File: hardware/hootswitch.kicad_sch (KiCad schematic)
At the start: 60 parts, among them J1 Mini-DIN-4-G, J2 Switch1, J7 Barrel_Jack_MountingPin, J8 POWER, J9 POWSEL, Q1 MMBT3904, Q2 MMBT3904, Q20 MMBT3904, Q3 MMBT3904, Q4 MMBT3904, Q5 MMBT3904, Q6 MMBT3904, Q7 MMBT3904, SW1 Switch1, U1 Pico, U14 LM1117-5.0

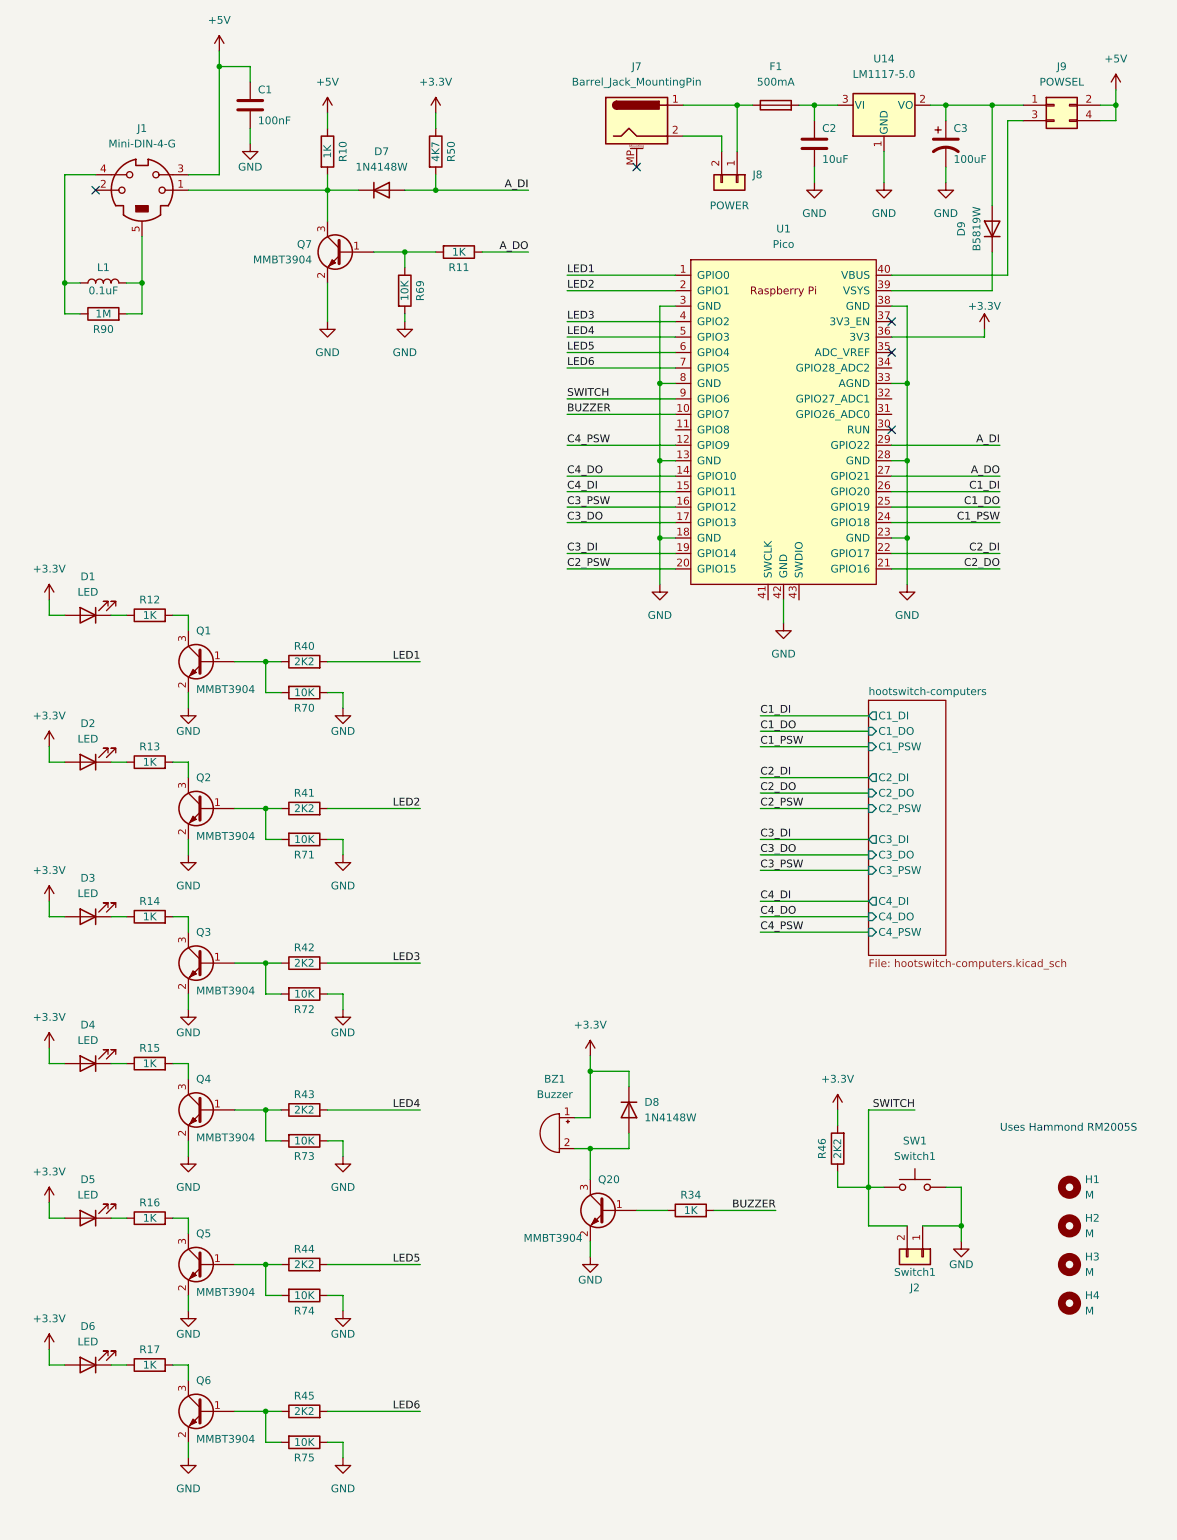
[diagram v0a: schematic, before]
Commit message: Switch to using proper digital isolator for data lines.
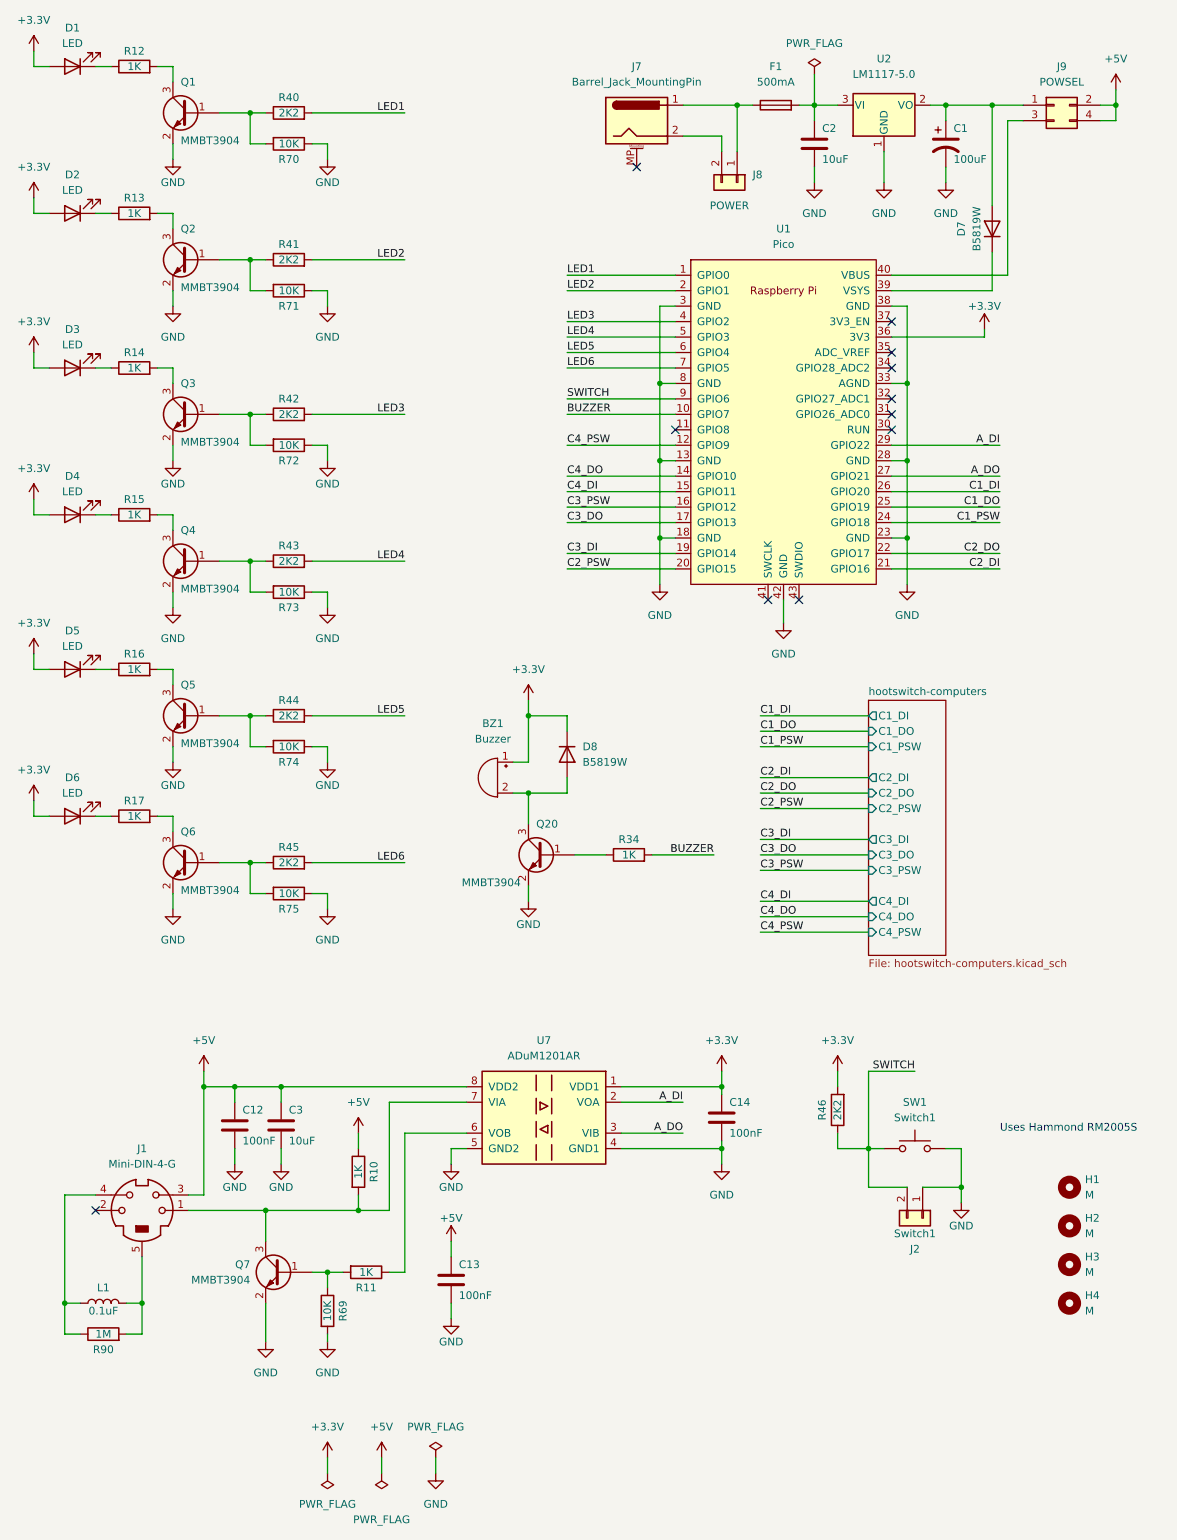
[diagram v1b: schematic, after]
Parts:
- removed D7: 1N4148W, Diode_SMD:D_SOD-123, symbol Diode:1N4148W
- removed R50: 4K7, Resistor_SMD:R_0603_1608Metric, symbol Device:R
- added C13, C14: 100nF, Capacitor_SMD:C_0603_1608Metric, symbol Device:C
- added C3: 10uF, Capacitor_SMD:C_0805_2012Metric, symbol Device:C
- added U7: ADuM1201AR, Package_SO:SOIC-8_3.9x4.9mm_P1.27mm, symbol Isolator:ADuM1201AR
- D8: value 1N4148W -> B5819W
- renumbered C3 to C1, C1 to C12, D9 to D7, U14 to U2
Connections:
- net +3.3V: now also C14.1, U7.1 (VDD1)
- net +5V: now also C13.1, C3.1, U7.8 (VDD2)
- net A_DI: now also U7.2 (VOA)
- net A_DO: now also U7.3 (VIB); no longer R11.1
- net C2_DI: now also U1.21 (GPIO16); no longer U1.22 (GPIO17)
- net C2_DO: now also U1.22 (GPIO17); no longer U1.21 (GPIO16)
- net GND: now also C13.2, C14.2, C3.2, U7.4 (GND1), U7.5 (GND2)
- net at J1.1, Q7.3 (C), R10.2: now also U7.7 (VIA)
- new net: R11.1, U7.6 (VOB)
- no-connect marks 5 -> 11
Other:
- moved on the sheet: BZ1, C12, D1, D2, D3, D4, D5, D6, D8, J1, J2, L1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

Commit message: Refinements for v2024a during BOM creation.
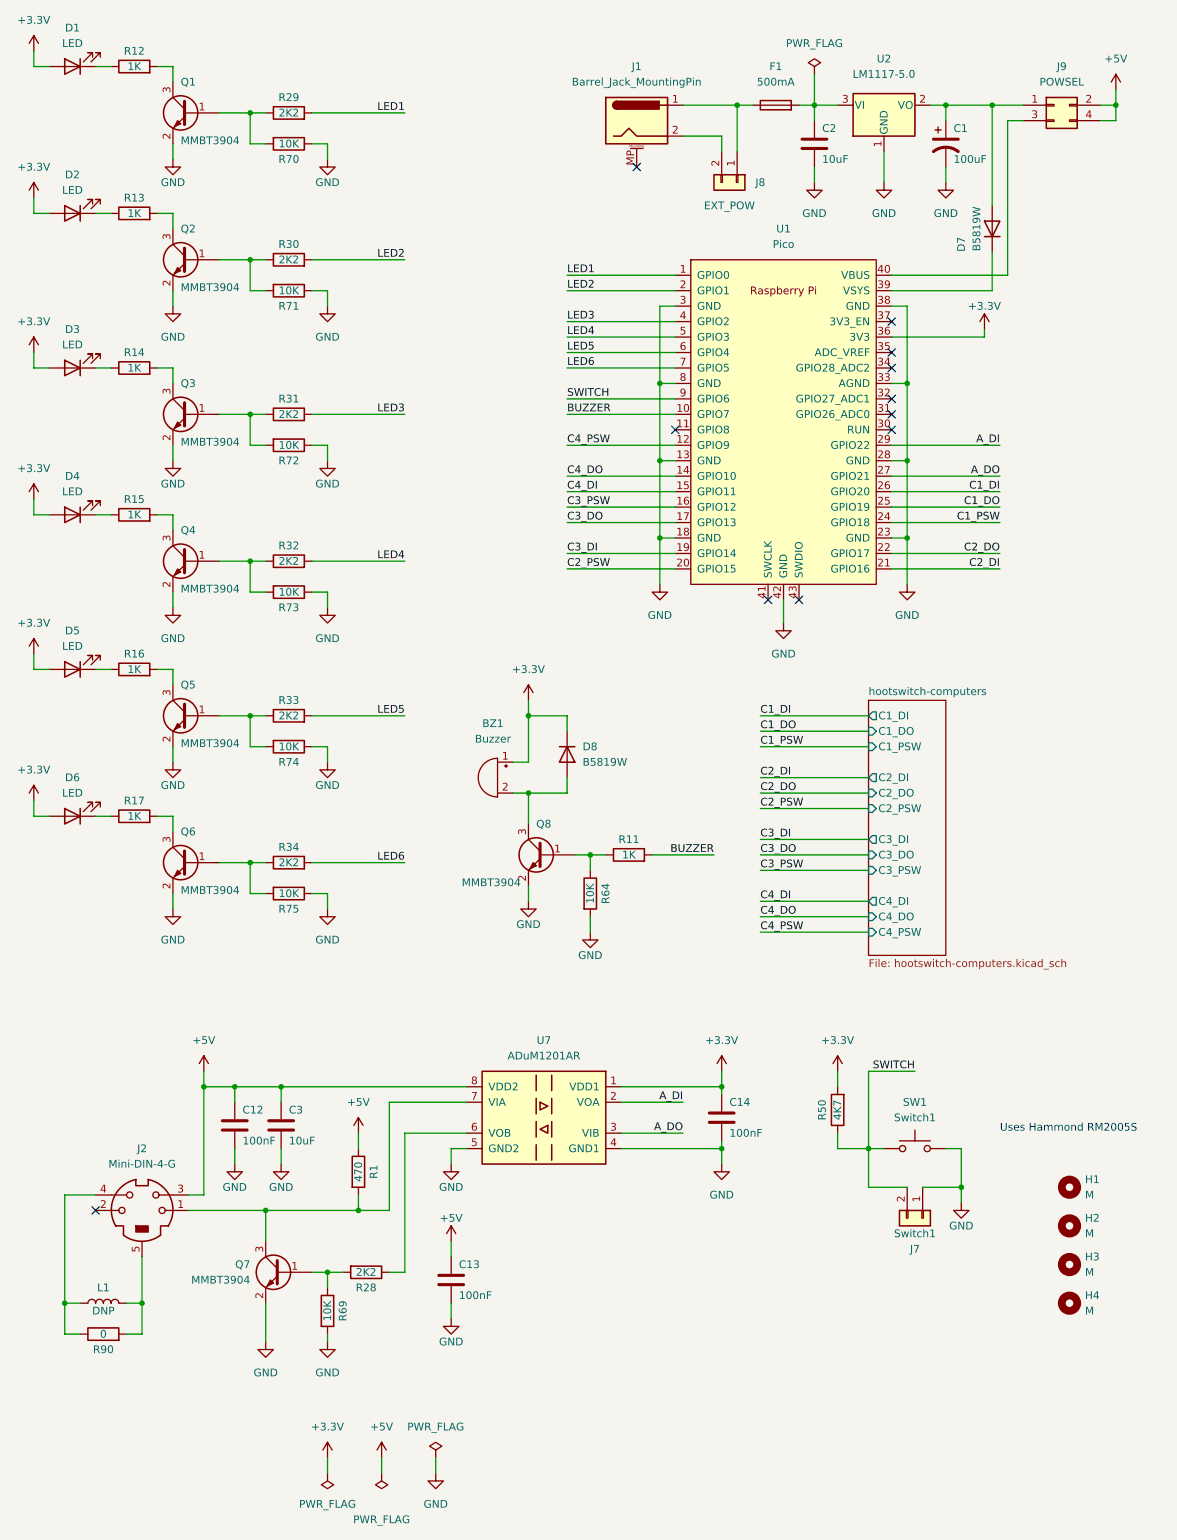
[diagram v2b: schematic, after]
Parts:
- added R64: 10K, Resistor_SMD:R_0603_1608Metric, symbol Device:R
- D7: symbol Simulation_SPICE:DIODE -> Device:D
- D8: symbol Diode:1N4148W -> Device:D
- J8: value POWER -> EXT_POW
- L1: value 0.1uF -> DNP
- R1: renamed from R10; value 1K -> 470
- R28: renamed from R11; value 1K -> 2K2
- R50: renamed from R46; value 2K2 -> 4K7
- R90: value 1M -> 0
- renumbered J7 to J1, J1 to J2, J2 to J7, Q20 to Q8, R34 to R11, R40 to R29, R41 to R30, R42 to R31, R43 to R32, R44 to R33, R45 to R34
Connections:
- net GND: now also R64.2
- net at C1.1, J9.1 (Pin_1), U2.2 (VO): now also D7.2 (A); no longer D7.1 (A)
- net at U1.39 (VSYS): now also D7.1 (K); no longer D7.2 (K)
- net at Q8.1 (B), R11.1: now also R64.1
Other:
- moved on the sheet: D7

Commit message: Add TWI and second DIN connector, update BOM.
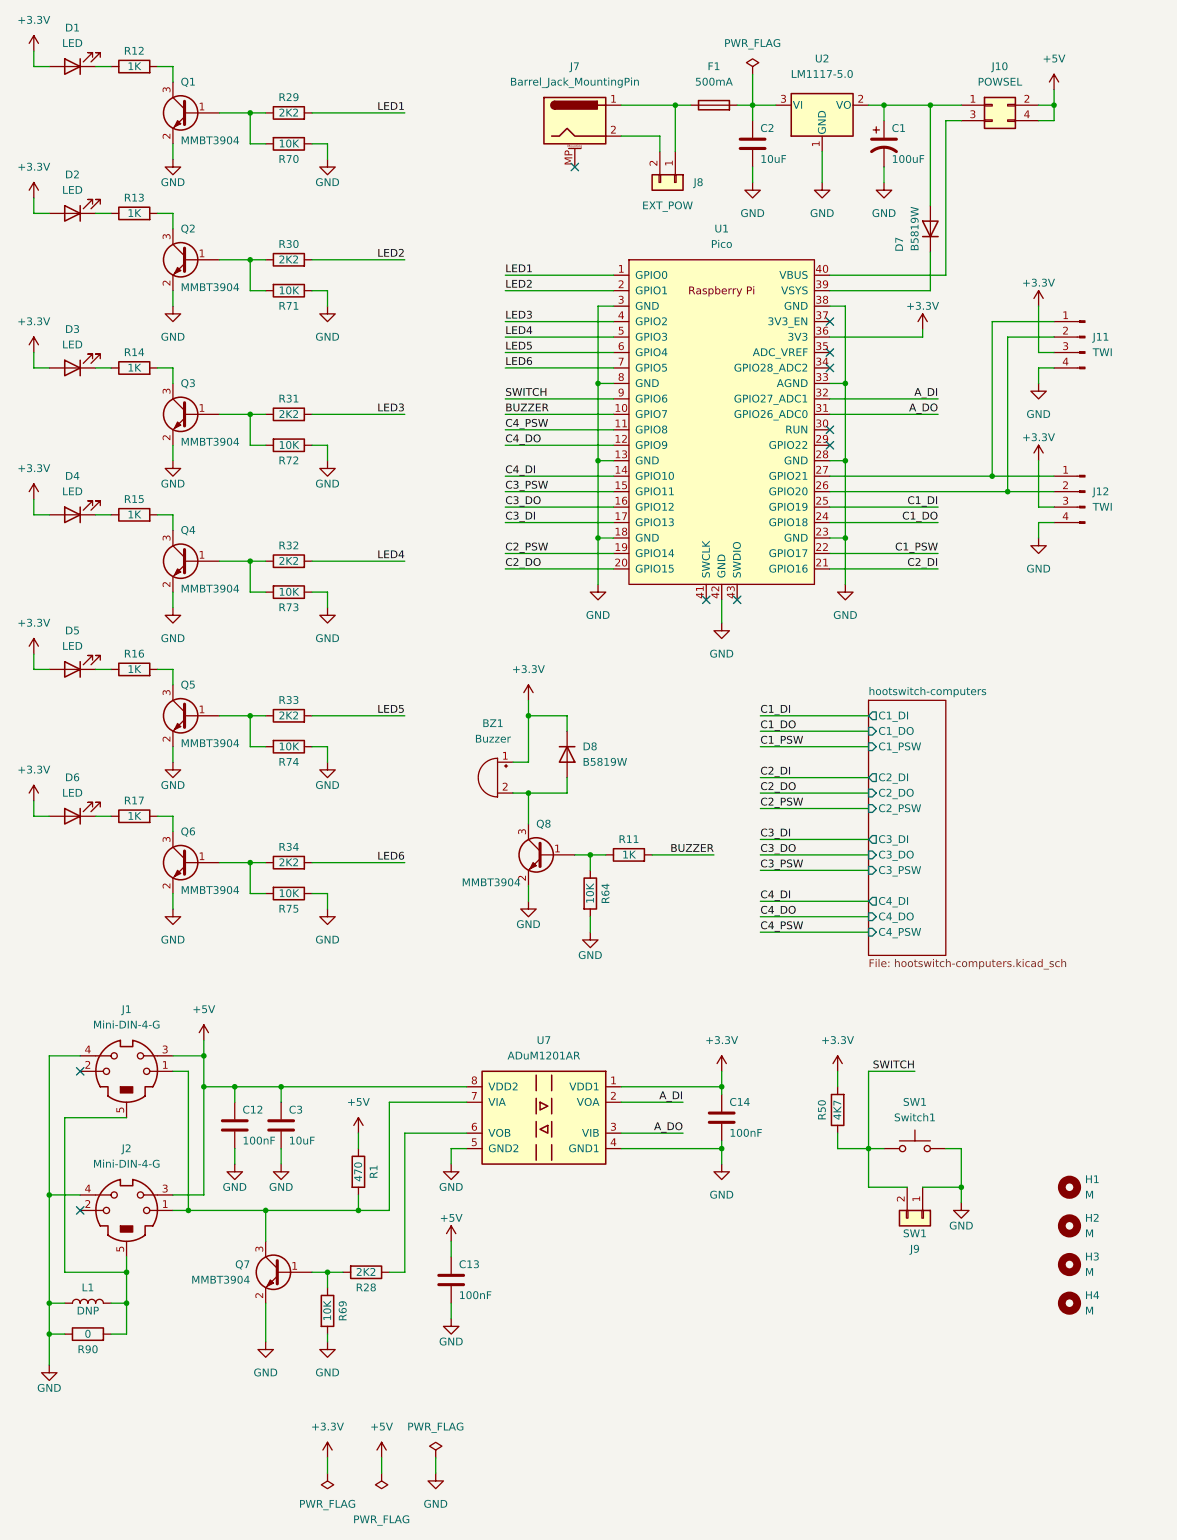
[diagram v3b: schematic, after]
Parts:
- added J1: Mini-DIN-4-G, hootswitch:5749181-1, symbol hootswitch:Mini-DIN-4-G
- added J11: TWI, Connector_JST:JST_SH_BM04B-SRSS-TB_1x04-1MP_P1.00mm_Vertical, symbol Connector:Conn_01x04_Male
- added J12: TWI, Connector_PinHeader_2.54mm:PinHeader_1x04_P2.54mm_Vertical, symbol Connector:Conn_01x04_Male
- J9: renamed from J7; value Switch1 -> SW1
- renumbered J9 to J10, J1 to J7
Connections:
- net +3.3V: now also J11.3 (Pin_3), J12.3 (Pin_3)
- net +5V: now also J1.3
- net A_DI: now also U1.32 (GPIO27_ADC1); no longer U1.29 (GPIO22)
- net A_DO: now also U1.31 (GPIO26_ADC0); no longer U1.27 (GPIO21)
- net C1_DI: now also U1.25 (GPIO19); no longer U1.26 (GPIO20)
- net C1_DO: now also U1.24 (GPIO18); no longer U1.25 (GPIO19)
- net C1_PSW: now also U1.22 (GPIO17); no longer U1.24 (GPIO18)
- net C2_DO: now also U1.20 (GPIO15); no longer U1.22 (GPIO17)
- net C2_PSW: now also U1.19 (GPIO14); no longer U1.20 (GPIO15)
- net C3_DI: now also U1.17 (GPIO13); no longer U1.19 (GPIO14)
- net C3_DO: now also U1.16 (GPIO12); no longer U1.17 (GPIO13)
- net C3_PSW: now also U1.15 (GPIO11); no longer U1.16 (GPIO12)
- net C4_DI: now also U1.14 (GPIO10); no longer U1.15 (GPIO11)
- net C4_DO: now also U1.12 (GPIO9); no longer U1.14 (GPIO10)
- net C4_PSW: now also U1.11 (GPIO8); no longer U1.12 (GPIO9)
- net GND: now also J2.4, L1.1, R90.1, J1.4, J11.4 (Pin_4), J12.4 (Pin_4)
- net at J2.1, Q7.3 (C), R1.2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: now also J1.1
- net at J2.5, L1.2, R90.2: now also J1.5
- new net: J11.1 (Pin_1), J12.1 (Pin_1), U1.27 (GPIO21)
- new net: J11.2 (Pin_2), J12.2 (Pin_2), U1.26 (GPIO20)
- no-connect marks 11 -> 10
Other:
- note removed: "Uses Hammond RM2005S"
- moved on the sheet: C1, C2, D7, F1, J10, J2, J7, J8, L1, R90, U1, U2

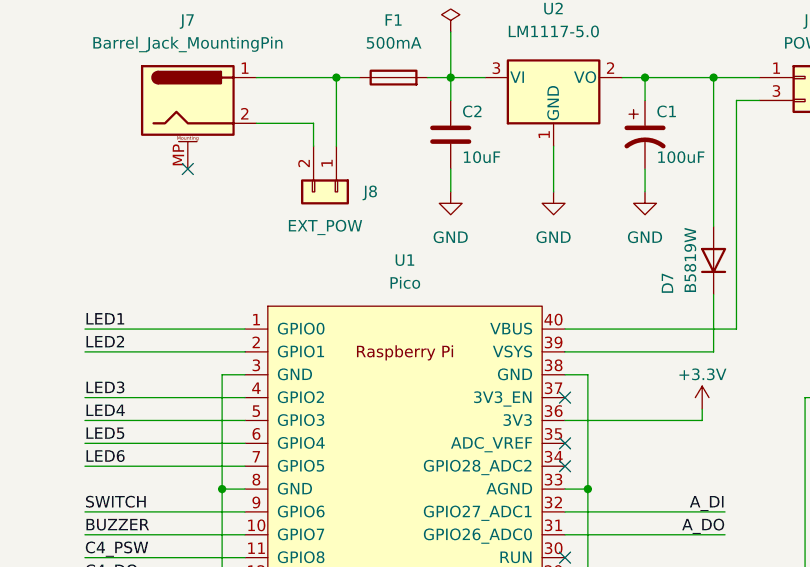
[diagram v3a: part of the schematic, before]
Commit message: Switch to using the RPi provided PicoW symbol and footprint.
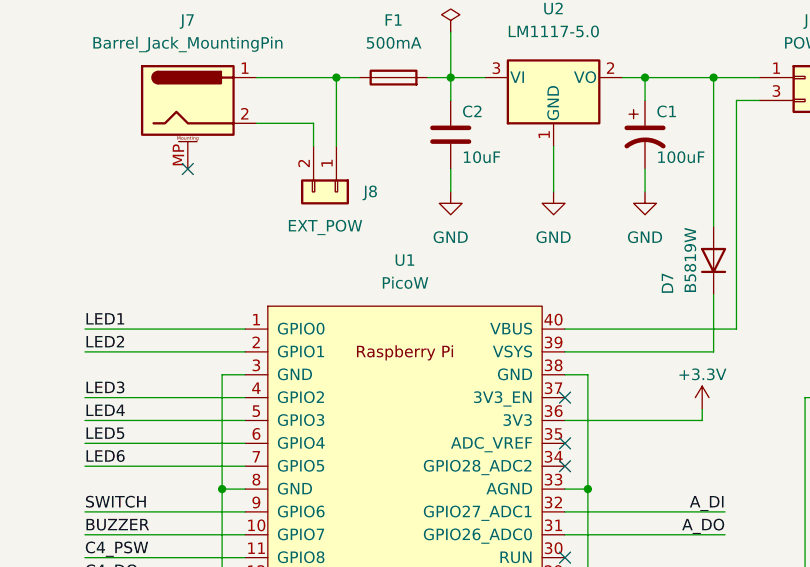
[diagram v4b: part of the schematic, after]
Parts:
- removed U1: Pico, MCU_RaspberryPi_and_Boards:RPi_Pico_SMD_TH, symbol MCU_RaspberryPi_and_Boards:Pico
- added U1: PicoW, RPi_Pico:RPi_PicoW_SMD_TH, symbol RPi_Pico:PicoW
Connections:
- net +3.3V: now also U1.36 (3V3)
- net A_DI: now also U1.32 (GPIO27_ADC1)
- net A_DO: now also U1.31 (GPIO26_ADC0)
- net BUZZER: now also U1.10 (GPIO7)
- net C1_DI: now also U1.25 (GPIO19)
- net C1_DO: now also U1.24 (GPIO18)
- net C1_PSW: now also U1.22 (GPIO17)
- net C2_DI: now also U1.21 (GPIO16)
- net C2_DO: now also U1.20 (GPIO15)
- net C2_PSW: now also U1.19 (GPIO14)
- net C3_DI: now also U1.17 (GPIO13)
- net C3_DO: now also U1.16 (GPIO12)
- net C3_PSW: now also U1.15 (GPIO11)
- net C4_DI: now also U1.14 (GPIO10)
- net C4_DO: now also U1.12 (GPIO9)
- net C4_PSW: now also U1.11 (GPIO8)
- net GND: now also U1.13 (GND), U1.18 (GND), U1.23 (GND), U1.28 (GND), U1.3 (GND), U1.33 (AGND), U1.38 (GND), U1.42 (GND), U1.8 (GND)
- net LED1: now also U1.1 (GPIO0)
- net LED2: now also U1.2 (GPIO1)
- net LED3: now also U1.4 (GPIO2)
- net LED4: now also U1.5 (GPIO3)
- net LED5: now also U1.6 (GPIO4)
- net LED6: now also U1.7 (GPIO5)
- net SWITCH: now also U1.9 (GPIO6)
- net at D7.1 (K): now also U1.39 (VSYS)
- net at J10.3 (Pin_3): now also U1.40 (VBUS)
- net at J11.1 (Pin_1), J12.1 (Pin_1): now also U1.27 (GPIO21)
- net at J11.2 (Pin_2), J12.2 (Pin_2): now also U1.26 (GPIO20)
